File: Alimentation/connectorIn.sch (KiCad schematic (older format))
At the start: 2 parts

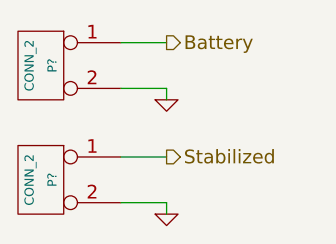
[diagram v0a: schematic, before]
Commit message: Adding board for alimentation
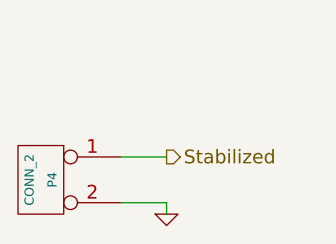
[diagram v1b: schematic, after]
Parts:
- removed P?: CONN_2, symbol CONN_2
- gave numbers to parts that had none: 1
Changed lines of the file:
@@
-EESchema Schematic File Version 2  date Thu 13 Mar 2014 12:12:56 CET
+EESchema Schematic File Version 2
 LIBS:power
 LIBS:device
@@
 LIBS:perso
 LIBS:alimentation-cache
-EELAYER 25  0
+EELAYER 24 0
 EELAYER END
-$Descr A4 11700 8267
+$Descr A4 11693 8268
 encoding utf-8
-Sheet 5 7
+Sheet 3 5
 Title ""
-Date "13 mar 2014"
+Date "20 mar 2014"
 Rev ""
 Comp ""
@@
 $EndDescr
 Wire Wire Line
-	1550 1750 1750 1750
-Wire Wire Line
 	1750 2500 1750 2450
 Wire Wire Line
@@
 Wire Wire Line
 	1750 2450 1550 2450
-Wire Wire Line
-	1550 1950 1750 1950
-Wire Wire Line
-	1750 1950 1750 2000
-Text HLabel 1750 1750 2    60   Output ~ 0
-Battery
 Text HLabel 1750 2250 2    60   Output ~ 0
 Stabilized
 $Comp
-L GND #PWR?
+L GND #PWR06
 U 1 1 53147E95
 P 1750 2500
-F 0 "#PWR?" H 1750 2500 30  0001 C CNN
+F 0 "#PWR06" H 1750 2500 30  0001 C CNN
 F 1 "GND" H 1750 2430 30  0001 C CNN
+F 2 "" H 1750 2500 60  0001 C CNN
+F 3 "" H 1750 2500 60  0001 C CNN
 	1    1750 2500
 	1    0    0    -1
 $EndComp
 $Comp
-L GND #PWR?
-U 1 1 53147E92
-P 1750 2000
-F 0 "#PWR?" H 1750 2000 30  0001 C CNN
-F 1 "GND" H 1750 1930 30  0001 C CNN
-	1    1750 2000
-	1    0    0    -1
-$EndComp
-$Comp
-L CONN_2 P?
+L CONN_2 P4
 U 1 1 53147E70
 P 1200 2350
-F 0 "P?" V 1150 2350 40  0000 C CNN
+F 0 "P4" V 1150 2350 40  0000 C CNN
 F 1 "CONN_2" V 1250 2350 40  0000 C CNN
+F 2 "" H 1200 2350 60  0001 C CNN
+F 3 "" H 1200 2350 60  0001 C CNN
 	1    1200 2350
 	-1   0    0    -1
 $EndComp
-$Comp
-L CONN_2 P?
-U 1 1 53147E62
-P 1200 1850
-F 0 "P?" V 1150 1850 40  0000 C CNN
-F 1 "CONN_2" V 1250 1850 40  0000 C CNN
-	1    1200 1850
-	-1   0    0    -1
-$EndComp

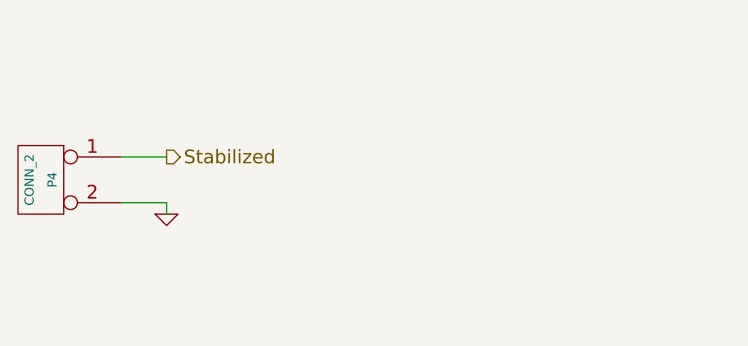
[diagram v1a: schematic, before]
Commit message: Debugging made on Alimentation, need thermal plan
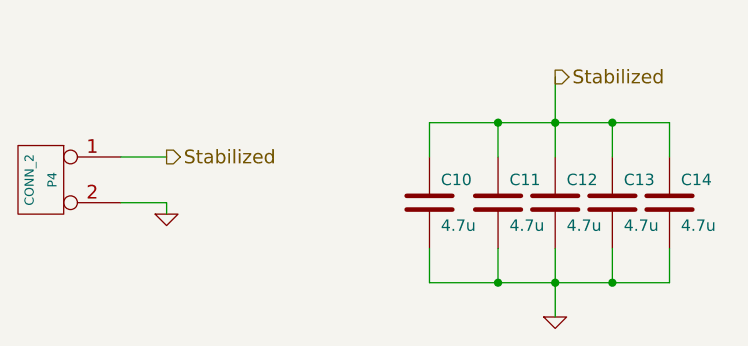
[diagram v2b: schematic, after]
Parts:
- added C10, C11, C12, C13, C14: 4.7u, symbol C
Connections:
- net GND: now also C10.2, C11.2, C12.2, C13.2, C14.2
- net Stabilized: now also C10.1, C11.1, C12.1, C13.1, C14.1
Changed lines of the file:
@@
 Stabilized
 $Comp
-L GND #PWR06
+L GND #PWR6
 U 1 1 53147E95
 P 1750 2500
-F 0 "#PWR06" H 1750 2500 30  0001 C CNN
+F 0 "#PWR6" H 1750 2500 30  0001 C CNN
 F 1 "GND" H 1750 2430 30  0001 C CNN
 F 2 "" H 1750 2500 60  0001 C CNN
@@
 	-1   0    0    -1
 $EndComp
+$Comp
+L C C10
+U 1 1 5379D5A0
+P 2900 2450
+F 0 "C10" H 2950 2550 50  0000 L CNN
+F 1 "4.7u" H 2950 2350 50  0000 L CNN
+F 2 "" H 2900 2450 60  0000 C CNN
+F 3 "" H 2900 2450 60  0000 C CNN
+	1    2900 2450
+	1    0    0    -1
+$EndComp
+$Comp
+L C C11
+U 1 1 5379D5AD
+P 3200 2450
+F 0 "C11" H 3250 2550 50  0000 L CNN
+F 1 "4.7u" H 3250 2350 50  0000 L CNN
+F 2 "" H 3200 2450 60  0000 C CNN
+F 3 "" H 3200 2450 60  0000 C CNN
+	1    3200 2450
+	1    0    0    -1
+$EndComp
+$Comp
+L C C12
+U 1 1 5379D5B3
+P 3450 2450
+F 0 "C12" H 3500 2550 50  0000 L CNN
+F 1 "4.7u" H 3500 2350 50  0000 L CNN
+F 2 "" H 3450 2450 60  0000 C CNN
+F 3 "" H 3450 2450 60  0000 C CNN
+	1    3450 2450
+	1    0    0    -1
+$EndComp
+$Comp
+L C C13
+U 1 1 5379D5B9
+P 3700 2450
+F 0 "C13" H 3750 2550 50  0000 L CNN
+F 1 "4.7u" H 3750 2350 50  0000 L CNN
+F 2 "" H 3700 2450 60  0000 C CNN
+F 3 "" H 3700 2450 60  0000 C CNN
+	1    3700 2450
+	1    0    0    -1
+$EndComp
+$Comp
+L C C14
+U 1 1 5379D5BF
+P 3950 2450
+F 0 "C14" H 4000 2550 50  0000 L CNN
+F 1 "4.7u" H 4000 2350 50  0000 L CNN
+F 2 "" H 3950 2450 60  0000 C CNN
+F 3 "" H 3950 2450 60  0000 C CNN
+	1    3950 2450
+	1    0    0    -1
+$EndComp
+Wire Wire Line
+	2900 2250 2900 2100
+Wire Wire Line
+	2900 2100 3950 2100
+Wire Wire Line
+	3950 2100 3950 2250
+Wire Wire Line
+	3700 2250 3700 2100
+Connection ~ 3700 2100
+Wire Wire Line
+	3450 1900 3450 2250
+Connection ~ 3450 2100
+Wire Wire Line
+	3200 2250 3200 2100
+Connection ~ 3200 2100
+Wire Wire Line
+	2900 2650 2900 2800
+Wire Wire Line
+	2900 2800 3950 2800
+Wire Wire Line
+	3950 2800 3950 2650
+Wire Wire Line
+	3200 2650 3200 2800
+Connection ~ 3200 2800
+Wire Wire Line
+	3450 2650 3450 2950
+Connection ~ 3450 2800
+Wire Wire Line
+	3700 2650 3700 2800
+Connection ~ 3700 2800
+$Comp
+L GND #PWR7
+U 1 1 5379D661
+P 3450 2950
+F 0 "#PWR7" H 3450 2950 30  0001 C CNN
+F 1 "GND" H 3450 2880 30  0001 C CNN
+F 2 "" H 3450 2950 60  0000 C CNN
+F 3 "" H 3450 2950 60  0000 C CNN
+	1    3450 2950
+	1    0    0    -1
+$EndComp
+Text HLabel 3450 1900 2    60   Output ~ 0
+Stabilized
 $EndSCHEMATC
